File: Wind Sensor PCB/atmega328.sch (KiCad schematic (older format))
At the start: 19 parts, among them P10 I2C, P3 ID, P4 ISP, P9 PROG, SW1 SWA, SW2 RST, U4 ATmega328P-AU, Y1 8MHz_XTAL

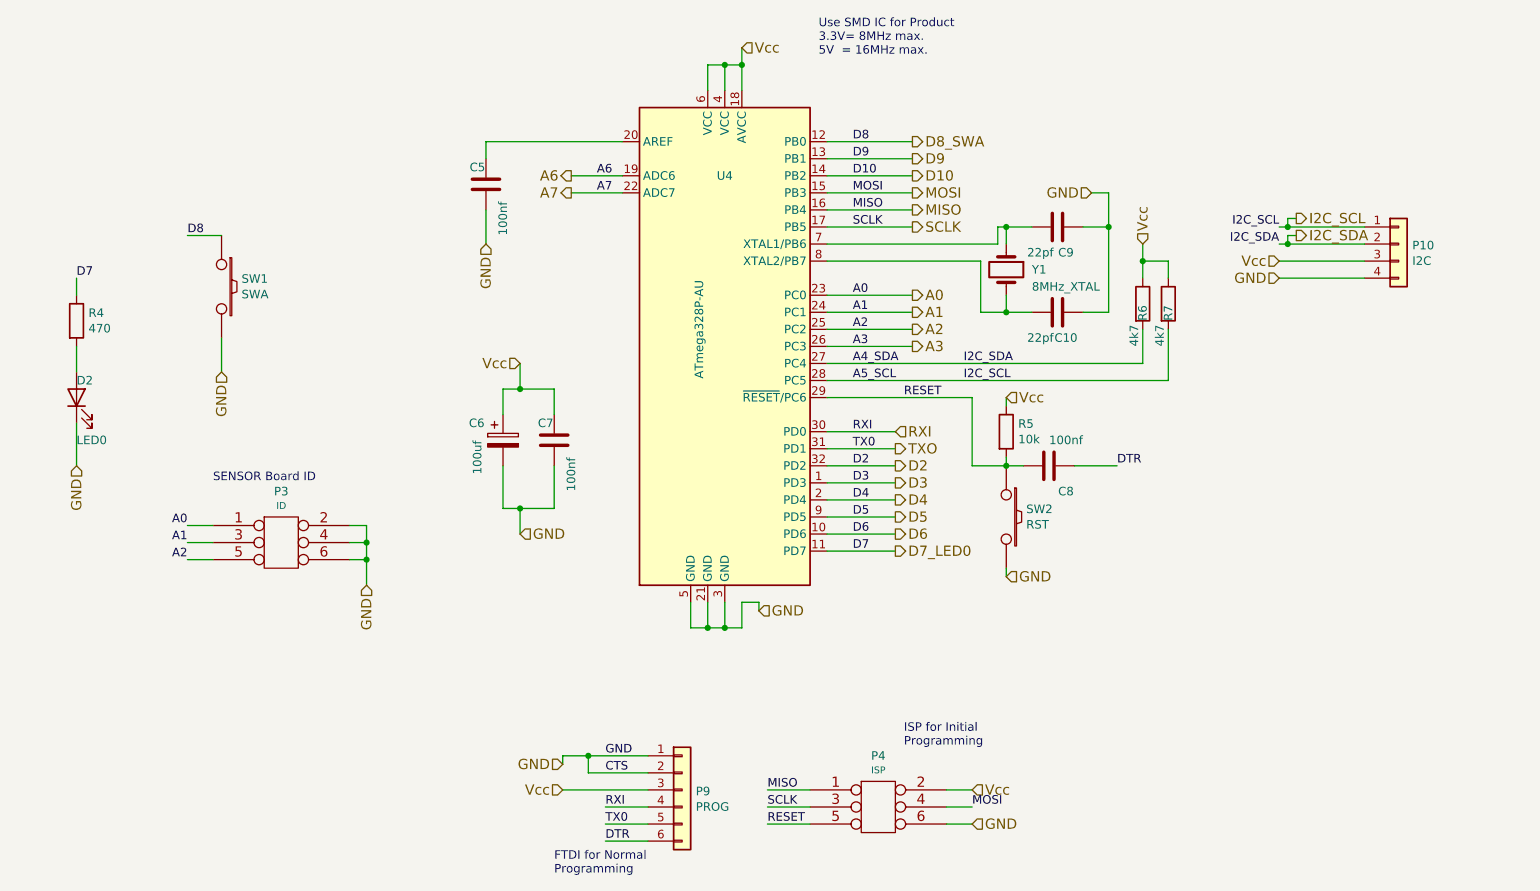
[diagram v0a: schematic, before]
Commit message: Updated PCB
Version 1 of the PCB with ATMEGA328 used...
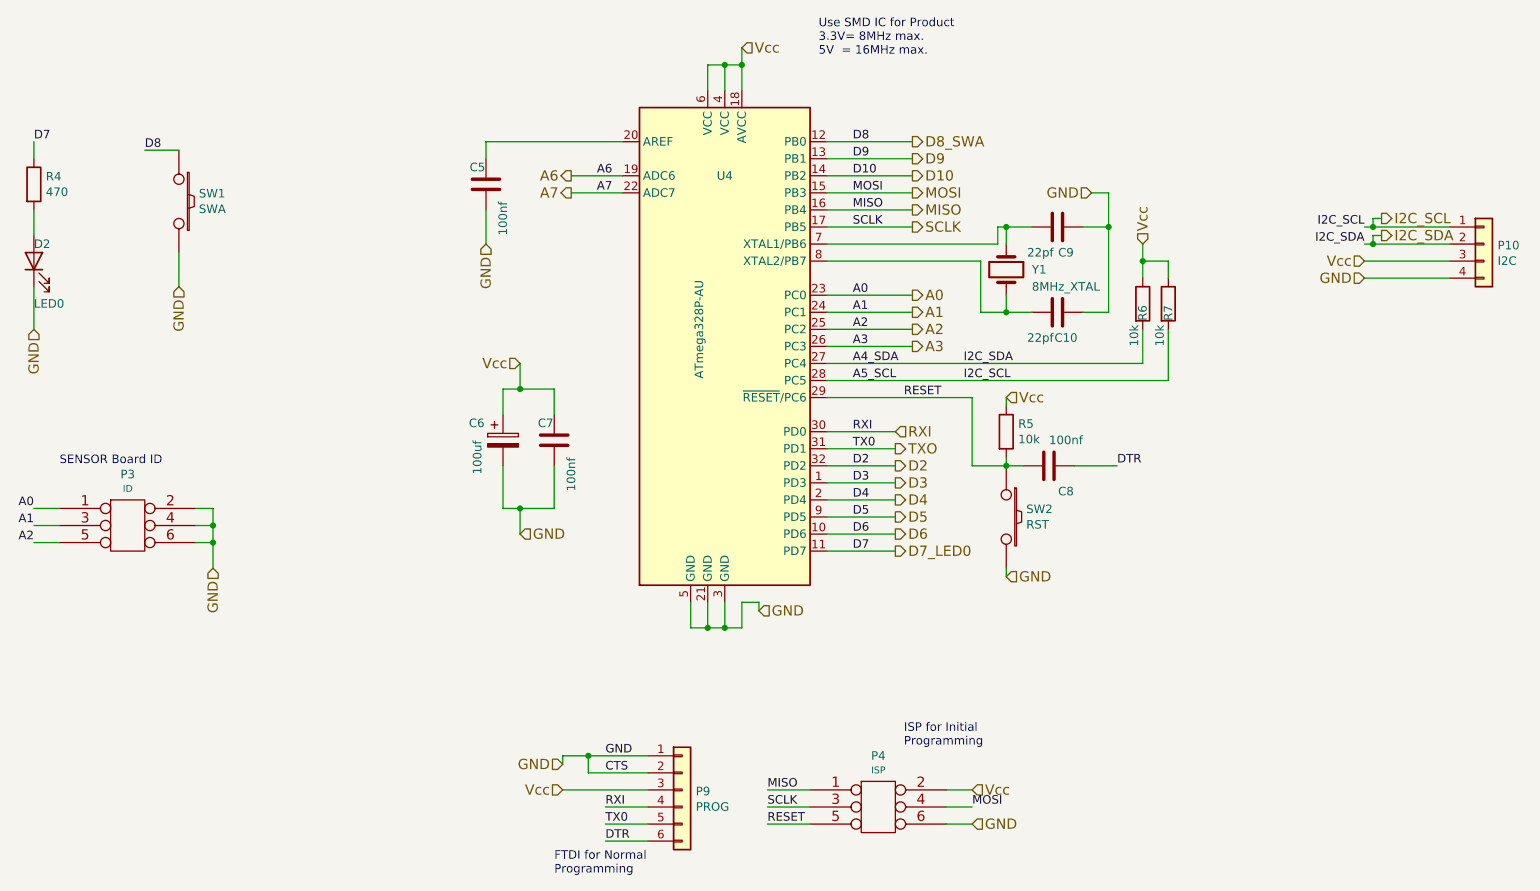
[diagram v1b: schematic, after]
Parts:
- R6, R7: value 4k7 -> 10k
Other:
- moved on the sheet: D2, P10, P3, R4, SW1

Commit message: large code update
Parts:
- C10, C9: value 22pf -> 22p; JLCPCB Add (none) -> Y; LCSC (none) -> C1804
- C5, C7, C8: value 100nf -> 100n; JLCPCB Add (none) -> Y; LCSC (none) -> C49678
- C6: value 100uf -> 100u; JLCPCB Add (none) -> Y; LCSC (none) -> C164071
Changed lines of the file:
@@
 AR Path="/60FFEE2F" Ref="R?"  Part="1"
 AR Path="/60FF06B8/60FFEE2F" Ref="R7"  Part="1"
-F 0 "R7" V 8200 2650 50  0000 L CNN
+F 0 "R7" V 8200 2700 50  0000 L CNN
 F 1 "10k" V 8150 2500 50  0000 L CNN
 F 2 "REInnovationFootprint:SM0805" V 8130 2750 50  0001 C CNN
@@
 AR Path="/60FFEF2E" Ref="R?"  Part="1"
 AR Path="/60FF06B8/60FFEF2E" Ref="R6"  Part="1"
-F 0 "R6" V 8050 2650 50  0000 L CNN
+F 0 "R6" V 8050 2700 50  0000 L CNN
 F 1 "10k" V 8000 2500 50  0000 L CNN
 F 2 "REInnovationFootprint:SM0805" V 7980 2750 50  0001 C CNN
@@
 P 7550 2800
 F 0 "C10" V 7700 2850 50  0000 C CNN
-F 1 "22pf" V 7700 2700 50  0000 C CNN
+F 1 "22p" V 7700 2700 50  0000 C CNN
 F 2 "REInnovationFootprint:SM_C_0805" H 7588 2650 50  0001 C CNN
 F 3 "~" H 7550 2800 50  0001 C CNN
+F 4 "C1804" H 7550 2800 50  0001 C CNN "LCSC"
+F 5 "Y" H 7550 2800 50  0001 C CNN "JLCPCB Add"
 	1    7550 2800
 	0    1    1    0
@@
 P 7550 2300
 F 0 "C9" V 7700 2350 50  0000 C CNN
-F 1 "22pf" V 7700 2200 50  0000 C CNN
+F 1 "22p" V 7700 2200 50  0000 C CNN
 F 2 "REInnovationFootprint:SM_C_0805" H 7588 2150 50  0001 C CNN
 F 3 "~" H 7550 2300 50  0001 C CNN
+F 4 "C1804" H 7550 2300 50  0001 C CNN "LCSC"
+F 5 "Y" H 7550 2300 50  0001 C CNN "JLCPCB Add"
 	1    7550 2300
 	0    1    1    0
@@
 P 7500 3700
 F 0 "C8" V 7650 3800 50  0000 C CNN
-F 1 "100nf" V 7350 3800 50  0000 C CNN
+F 1 "100n" V 7350 3800 50  0000 C CNN
 F 2 "REInnovationFootprint:SM_C_0805" H 7538 3550 50  0001 C CNN
 F 3 "~" H 7500 3700 50  0001 C CNN
+F 4 "C49678" H 7500 3700 50  0001 C CNN "LCSC"
+F 5 "Y" H 7500 3700 50  0001 C CNN "JLCPCB Add"
 	1    7500 3700
 	0    1    1    0
@@
 P 4600 3550
 F 0 "C7" H 4650 3450 50  0000 C CNN
-F 1 "100nf" V 4500 3750 50  0000 C CNN
+F 1 "100n" V 4500 3750 50  0000 C CNN
 F 2 "REInnovationFootprint:SM_C_0805" H 4638 3400 50  0001 C CNN
 F 3 "~" H 4600 3550 50  0001 C CNN
+F 4 "C49678" H 4600 3550 50  0001 C CNN "LCSC"
+F 5 "Y" H 4600 3550 50  0001 C CNN "JLCPCB Add"
 	1    4600 3550
 	-1   0    0    1
@@
 P 4300 3550
 F 0 "C6" H 4100 3650 50  0000 L CNN
-F 1 "100uf" V 4150 3350 50  0000 L CNN
+F 1 "100u" V 4150 3350 50  0000 L CNN
 F 2 "REInnovationFootprint:SM_6.3x7.7" H 4338 3400 50  0001 C CNN
 F 3 "~" H 4300 3550 50  0001 C CNN
+F 4 "C164071" H 4300 3550 50  0001 C CNN "LCSC"
+F 5 "Y" H 4300 3550 50  0001 C CNN "JLCPCB Add"
 	1    4300 3550
 	1    0    0    -1
@@
 P 4200 2050
 F 0 "C5" H 4250 1950 50  0000 C CNN
-F 1 "100nf" V 4100 2250 50  0000 C CNN
+F 1 "100n" V 4100 2250 50  0000 C CNN
 F 2 "REInnovationFootprint:SM_C_0805" H 4238 1900 50  0001 C CNN
 F 3 "~" H 4200 2050 50  0001 C CNN
+F 4 "C49678" H 4200 2050 50  0001 C CNN "LCSC"
+F 5 "Y" H 4200 2050 50  0001 C CNN "JLCPCB Add"
 	1    4200 2050
 	-1   0    0    1
